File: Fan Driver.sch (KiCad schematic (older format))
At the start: 0 parts

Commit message: Added Relay and Fan subsystem block diagrams
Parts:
- added Q?: MOSFET_N, ~, symbol MOSFET_N
- added R? (x5): R, ~, symbol R
- added RV?: POT, ~, symbol POT
- added U?: LM324, symbol LM324
- added U?: MCP4922-E/P, DIP14, symbol MCP4922-E/P
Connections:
- net labels added: +12V, -12V, AGND, CS_N, Current Measure, MISO, MOSI, SCLK
- wire segments 0 -> 37

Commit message: Blocked out the LED Driver and Power sheets
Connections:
- wire segments 37 -> 38
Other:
- moved on the sheet: Q?, R?, U?, U?A

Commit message: Completed Arduino Block Diagram and Fan Redesign
The commits as of this are now up to date with the videos released for
Contextual Electronics, Week 3.
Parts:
- removed R? (x3): R, ~, symbol R
- removed RV?: POT, ~, symbol POT
- added D?: DIODE, ~, symbol DIODE
- added Q? (x2): MOSFET_N, ~, symbol MOSFET_N
- added TH?: THERMISTOR, ~, symbol THERMISTOR
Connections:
- net labels added: +12C, CURR_MEAS, FAN_MODE, FAN_OUT+, FAN_OUT-, FAN_PWM, TACH_IN, TACH_MEAS
- net labels removed: Current Measure, FAN_IN, POWER +, POWER -, TACH, TACH_OUT
- wire segments 38 -> 39
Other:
- moved on the sheet: Q?, R?, U?, U?A

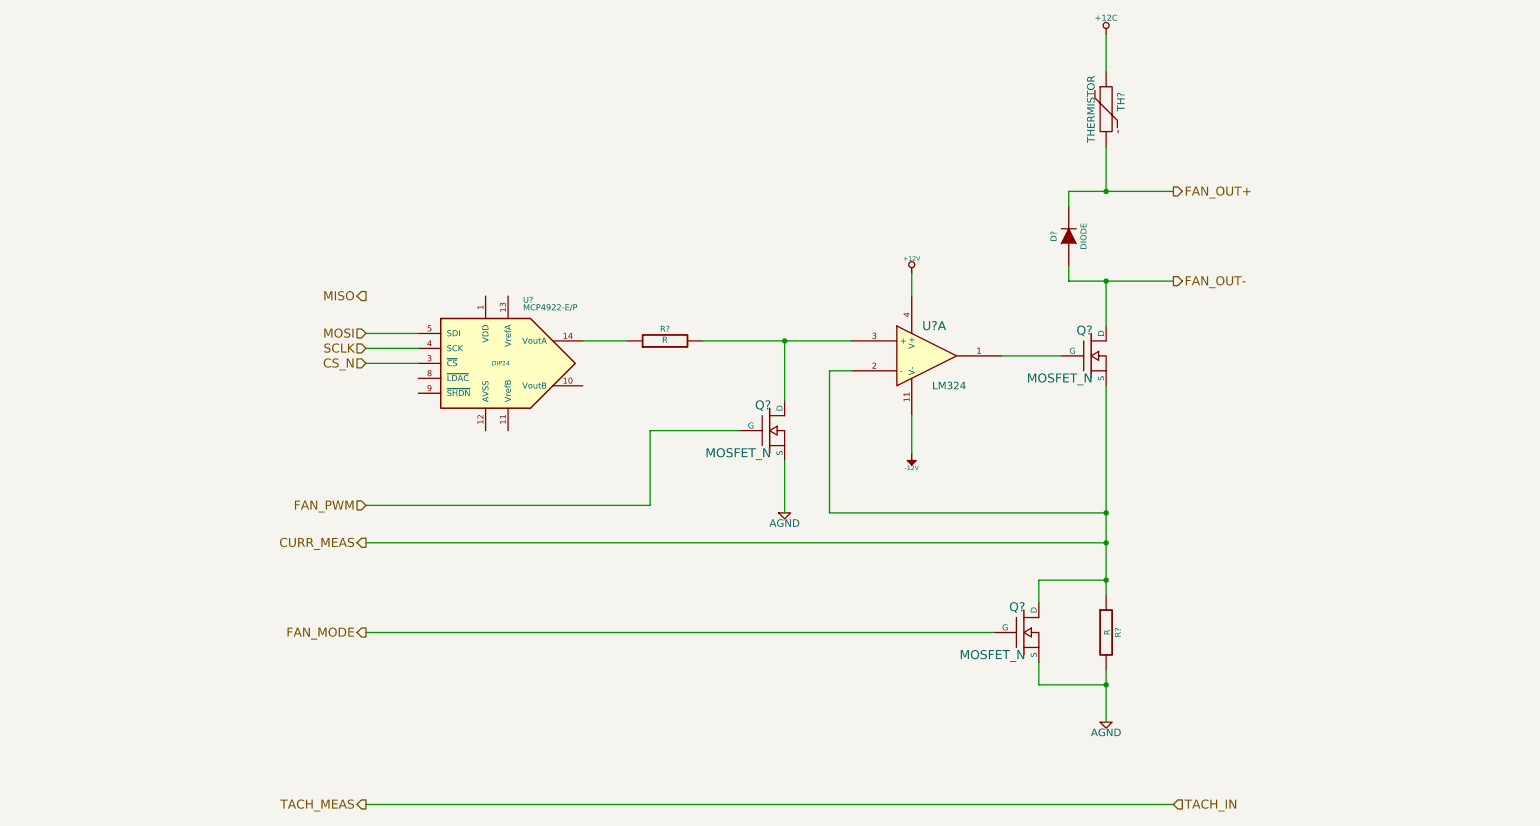
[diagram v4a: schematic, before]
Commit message: Initial layout of relay and thermocouple
All block diagrams completed through Week 3.  Component selection
spreadsheets created: Bench Buddy Session 1CE.xlsx = official part
selection and bom.xlsx is the version I came up with.

Part association and initial layout of the Relay and Thermocouple
sections completed.
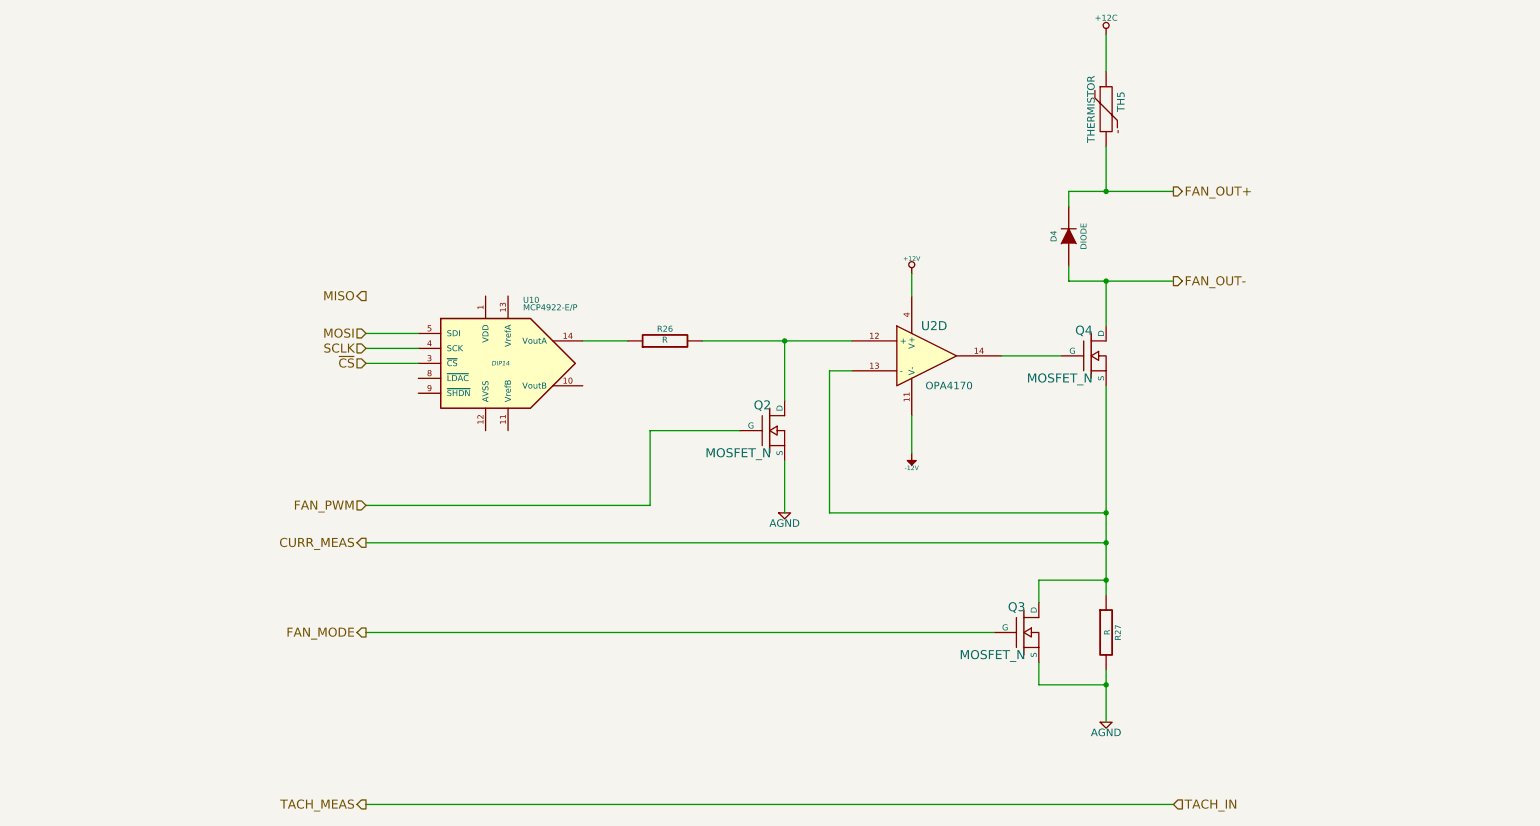
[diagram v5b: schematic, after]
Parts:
- U2: renamed from U?; value LM324 -> OPA4170; Distrib Part Num 1 (none) -> 296-29664-1; Distrib Part Num 1 Link (none) -> http://www.digikey.com/product-detail/en/OPA4170AIDR/296-29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; MFG Name (none) -> Texas Instruments; MFG Part Num (none) -> OPA4170AIDR
- gave numbers to parts that had none: 8
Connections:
- net CURR_MEAS: now also U2.13 (-); no longer U2.2 (-)
- net at Q4.1 (G): now also U2.14; no longer U2.1
- net at Q2.2 (D), R26.2: now also U2.12 (+); no longer U2.3 (+)
- net CS_N renamed ~CS
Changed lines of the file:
@@
 Sheet 7 9
 Title ""
-Date "6 feb 2014"
+Date "21 feb 2014"
 Rev ""
 Comp ""
@@
 FAN_PWM
 $Comp
-L LM324 U?
-U 1 1 52F27A1B
+L LM324 U2
+U 4 1 52F27A1B
 P 6850 3500
-F 0 "U?" H 6900 3700 60  0000 C CNN
-F 1 "LM324" H 7000 3300 50  0000 C CNN
+F 0 "U2" H 6900 3700 60  0000 C CNN
+F 1 "OPA4170" H 7000 3300 50  0000 C CNN
 F 2 "" H 6850 3500 60  0000 C CNN
 F 3 "" H 6850 3500 60  0000 C CNN
-	1    6850 3500
-	1    0    0    -1
-$EndComp
-$Comp
-L MOSFET_N Q?
+F 4 "Texas Instruments" H 6850 3500 60  0001 C CNN "MFG Name"
+F 5 "OPA4170AIDR" H 6850 3500 60  0001 C CNN "MFG Part Num"
+F 6 "296-29664-1" H 6850 3500 60  0001 C CNN "Distrib Part Num 1"
+F 7 "http://www.digikey.com/product-detail/en/OPA4170AIDR/296-29664-1-ND/2762167" H 6850 3500 60  0001 C CNN "Distrib Part Num 1 Link"
+	4    6850 3500
+	1    0    0    -1
+$EndComp
+$Comp
+L MOSFET_N Q4
 U 1 1 52F27A2A
 P 7950 3500
-F 0 "Q?" H 7960 3670 60  0000 R CNN
+F 0 "Q4" H 7960 3670 60  0000 R CNN
 F 1 "MOSFET_N" H 7960 3350 60  0000 R CNN
 F 2 "~" H 7950 3500 60  0000 C CNN
@@
 $EndComp
 $Comp
-L R R?
+L R R27
 U 1 1 52F27A50
 P 8050 5350
-F 0 "R?" V 8130 5350 40  0000 C CNN
+F 0 "R27" V 8130 5350 40  0000 C CNN
 F 1 "R" V 8057 5351 40  0000 C CNN
 F 2 "~" V 7980 5350 30  0000 C CNN
@@
 $EndComp
 $Comp
-L AGND #PWR?
+L AGND #PWR048
 U 1 1 52F27A5F
 P 8050 5950
-F 0 "#PWR?" H 8050 5950 40  0001 C CNN
+F 0 "#PWR048" H 8050 5950 40  0001 C CNN
 F 1 "AGND" H 8050 5880 50  0000 C CNN
 F 2 "" H 8050 5950 60  0000 C CNN
@@
 $EndComp
 $Comp
-L +12V #PWR?
+L +12V #PWR049
 U 1 1 52F27A88
 P 6750 2950
-F 0 "#PWR?" H 6750 2900 20  0001 C CNN
+F 0 "#PWR049" H 6750 2900 20  0001 C CNN
 F 1 "+12V" H 6750 3050 30  0000 C CNN
 F 2 "" H 6750 2950 60  0000 C CNN
@@
 $EndComp
 $Comp
-L -12V #PWR?
+L -12V #PWR050
 U 1 1 52F27A9B
 P 6750 4150
-F 0 "#PWR?" H 6750 4280 20  0001 C CNN
+F 0 "#PWR050" H 6750 4280 20  0001 C CNN
 F 1 "-12V" H 6750 4250 30  0000 C CNN
 F 2 "" H 6750 4150 60  0000 C CNN
@@
 $EndComp
 $Comp
-L AGND #PWR?
+L AGND #PWR051
 U 1 1 52F27AFD
 P 5900 4550
-F 0 "#PWR?" H 5900 4550 40  0001 C CNN
+F 0 "#PWR051" H 5900 4550 40  0001 C CNN
 F 1 "AGND" H 5900 4480 50  0000 C CNN
 F 2 "" H 5900 4550 60  0000 C CNN
@@
 $EndComp
 $Comp
-L MCP4922-E/P U?
+L MCP4922-E/P U10
 U 1 1 52F27B2C
 P 4000 3550
-F 0 "U?" H 4150 3950 40  0000 L BNN
+F 0 "U10" H 4150 3950 40  0000 L BNN
 F 1 "MCP4922-E/P" H 4150 3900 40  0000 L BNN
 F 2 "DIP14" H 4000 3550 30  0000 C CIN
@@
 CURR_MEAS
 $Comp
-L R R?
+L R R26
 U 1 1 52F27BDB
 P 5100 3400
-F 0 "R?" V 5180 3400 40  0000 C CNN
+F 0 "R26" V 5180 3400 40  0000 C CNN
 F 1 "R" V 5107 3401 40  0000 C CNN
 F 2 "~" V 5030 3400 30  0000 C CNN
@@
 MISO
 Text HLabel 3100 3550 0    60   Input ~ 0
-CS_N
+~CS
 Text HLabel 3100 3450 0    60   Input ~ 0
 SCLK
 $Comp
-L MOSFET_N Q?
+L MOSFET_N Q3
 U 1 1 52F3FFDA
 P 7500 5350
-F 0 "Q?" H 7510 5520 60  0000 R CNN
+F 0 "Q3" H 7510 5520 60  0000 R CNN
 F 1 "MOSFET_N" H 7510 5200 60  0000 R CNN
 F 2 "~" H 7500 5350 60  0000 C CNN
@@
 $EndComp
 $Comp
-L THERMISTOR TH?
+L THERMISTOR TH5
 U 1 1 52F40000
 P 8050 1850
-F 0 "TH?" V 8150 1900 50  0000 C CNN
+F 0 "TH5" V 8150 1900 50  0000 C CNN
 F 1 "THERMISTOR" V 7950 1850 50  0000 C CNN
 F 2 "~" H 8050 1850 60  0000 C CNN
@@
 $EndComp
 $Comp
-L DIODE D?
+L DIODE D4
 U 1 1 52F40093
 P 7800 2700
-F 0 "D?" H 7800 2800 40  0000 C CNN
+F 0 "D4" H 7800 2800 40  0000 C CNN
 F 1 "DIODE" H 7800 2600 40  0000 C CNN
 F 2 "~" H 7800 2700 60  0000 C CNN
@@
 	8050 3000 8050 3300
 Wire Wire Line
-	7800 3000 8050 3000
-Wire Wire Line
-	8050 3000 8500 3000
-Wire Wire Line
-	7800 2400 8050 2400
-Wire Wire Line
-	8050 2400 8500 2400
+	7800 3000 8500 3000
+Wire Wire Line
+	7800 2400 8500 2400
 Wire Wire Line
 	8050 2100 8050 2400
@@
 	5900 4200 5900 4550
 Wire Wire Line
-	5350 3400 5900 3400
-Wire Wire Line
-	5900 3400 6350 3400
+	5350 3400 6350 3400
 Wire Wire Line
 	6750 3900 6750 4150
@@
 	6200 4550 6200 3600
 Wire Wire Line
-	8050 5600 8050 5700
-Wire Wire Line
-	8050 5700 8050 5950
-Wire Wire Line
-	8050 3700 8050 4550
-Wire Wire Line
-	8050 4550 8050 4750
-Wire Wire Line
-	8050 4750 8050 5000
-Wire Wire Line
-	8050 5000 8050 5100
+	8050 5600 8050 5950
+Wire Wire Line
+	8050 3700 8050 5100
 Wire Wire Line
 	6200 4550 8050 4550
@@
 	7750 3500 7350 3500
 $Comp
-L MOSFET_N Q?
+L MOSFET_N Q2
 U 1 1 52F4044A
 P 5800 4000
-F 0 "Q?" H 5810 4170 60  0000 R CNN
+F 0 "Q2" H 5810 4170 60  0000 R CNN
 F 1 "MOSFET_N" H 5810 3850 60  0000 R CNN
 F 2 "~" H 5800 4000 60  0000 C CNN
@@
 FAN_MODE
 $Comp
-L +12C #PWR?
+L +12C #PWR052
 U 1 1 52F40CFB
 P 8050 1350
-F 0 "#PWR?" H 8050 1320 30  0001 C CNN
+F 0 "#PWR052" H 8050 1320 30  0001 C CNN
 F 1 "+12C" H 8050 1460 40  0000 C CNN
 F 2 "" H 8050 1350 60  0000 C CNN
